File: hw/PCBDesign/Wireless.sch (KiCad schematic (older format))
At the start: 5 parts

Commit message: Clean up schematics some
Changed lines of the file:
@@
 Text HLabel 6300 1100 1    50   Input ~ 0
 V+
+Text HLabel 4550 3600 2    50   Input ~ 0
+BT_VCC_EN
+Text HLabel 4200 1000 0    50   Input ~ 0
+RF24_VCC_EN
 $EndSCHEMATC

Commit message: Schematic polishing
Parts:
- C34: renamed from C?; footprint (none) -> Capacitor_SMD:C_0805_2012Metric; LCSC (none) -> C28323
- C35: renamed from C?; value 100nF -> 100n; footprint (none) -> Capacitor_SMD:C_0402_1005Metric; LCSC (none) -> C1525
- R70, R71: renamed from R?; footprint (none) -> Resistor_SMD:R_0402_1005Metric; LCSC (none) -> C25744
- gave numbers to parts that had none: 1
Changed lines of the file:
@@
 $EndDescr
 $Comp
-L RF:NRF24L01_Breakout U?
+L RF:NRF24L01_Breakout U6
 U 1 1 60458E2E
 P 6300 1700
-F 0 "U?" H 6650 2300 50  0000 L CNN
+F 0 "U6" H 6650 2300 50  0000 L CNN
 F 1 "NRF24L01_Breakout" H 6350 2200 50  0000 L CNN
 F 2 "RF_Module:nRF24L01_Breakout" H 6450 2300 50  0001 L CIN
@@
 nRF24_IRQ
 $Comp
-L power:GND #PWR?
+L power:GND #PWR076
 U 1 1 60625E14
 P 6300 2300
-F 0 "#PWR?" H 6300 2050 50  0001 C CNN
+F 0 "#PWR076" H 6300 2050 50  0001 C CNN
 F 1 "GND" H 6305 2127 50  0000 C CNN
 F 2 "" H 6300 2300 50  0001 C CNN
@@
 nRF24_IRQ
 $Comp
-L Device:C C?
+L Device:C C34
 U 1 1 606288B3
 P 8300 1750
-F 0 "C?" H 8415 1796 50  0000 L CNN
+F 0 "C34" H 8415 1796 50  0000 L CNN
 F 1 "10uF" H 8415 1705 50  0000 L CNN
-F 2 "" H 8338 1600 50  0001 C CNN
+F 2 "Capacitor_SMD:C_0805_2012Metric" H 8338 1600 50  0001 C CNN
 F 3 "~" H 8300 1750 50  0001 C CNN
+F 4 "C28323" H 8300 1750 50  0001 C CNN "LCSC"
 	1    8300 1750
 	1    0    0    -1
 $EndComp
 $Comp
-L Device:C C?
+L Device:C C35
 U 1 1 60628CEA
 P 8700 1750
-F 0 "C?" H 8815 1796 50  0000 L CNN
-F 1 "100nF" H 8815 1705 50  0000 L CNN
-F 2 "" H 8738 1600 50  0001 C CNN
+F 0 "C35" H 8815 1796 50  0000 L CNN
+F 1 "100n" H 8815 1705 50  0000 L CNN
+F 2 "Capacitor_SMD:C_0402_1005Metric" H 8738 1600 50  0001 C CNN
 F 3 "~" H 8700 1750 50  0001 C CNN
+F 4 "C1525" H 8700 1750 50  0001 C CNN "LCSC"
 	1    8700 1750
 	1    0    0    -1
 $EndComp
 $Comp
-L Device:R_US R?
+L Device:R_US R71
 U 1 1 60628F56
 P 7750 1800
-F 0 "R?" H 7818 1846 50  0000 L CNN
+F 0 "R71" H 7818 1846 50  0000 L CNN
 F 1 "10k" H 7818 1755 50  0000 L CNN
-F 2 "" V 7790 1790 50  0001 C CNN
+F 2 "Resistor_SMD:R_0402_1005Metric" V 7790 1790 50  0001 C CNN
 F 3 "~" H 7750 1800 50  0001 C CNN
+F 4 "C25744" H 7750 1800 50  0001 C CNN "LCSC"
 	1    7750 1800
 	0    1    1    0
@@
 	8300 1600 8300 1500
 $Comp
-L power:GND #PWR?
+L power:GND #PWR077
 U 1 1 60629A72
 P 8300 1900
-F 0 "#PWR?" H 8300 1650 50  0001 C CNN
+F 0 "#PWR077" H 8300 1650 50  0001 C CNN
 F 1 "GND" H 8305 1727 50  0000 C CNN
 F 2 "" H 8300 1900 50  0001 C CNN
@@
 $EndComp
 $Comp
-L power:GND #PWR?
+L power:GND #PWR078
 U 1 1 60629F1D
 P 8700 1900
-F 0 "#PWR?" H 8700 1650 50  0001 C CNN
+F 0 "#PWR078" H 8700 1650 50  0001 C CNN
 F 1 "GND" H 8705 1727 50  0000 C CNN
 F 2 "" H 8700 1900 50  0001 C CNN
@@
 	7600 1800 7400 1800
 $Comp
-L Device:R_US R?
+L Device:R_US R70
 U 1 1 6062A636
 P 7750 1500
-F 0 "R?" H 7818 1546 50  0000 L CNN
+F 0 "R70" H 7818 1546 50  0000 L CNN
 F 1 "10k" H 7818 1455 50  0000 L CNN
-F 2 "" V 7790 1490 50  0001 C CNN
+F 2 "Resistor_SMD:R_0402_1005Metric" V 7790 1490 50  0001 C CNN
 F 3 "~" H 7750 1500 50  0001 C CNN
+F 4 "C25744" H 7750 1500 50  0001 C CNN "LCSC"
 	1    7750 1500
 	0    1    1    0

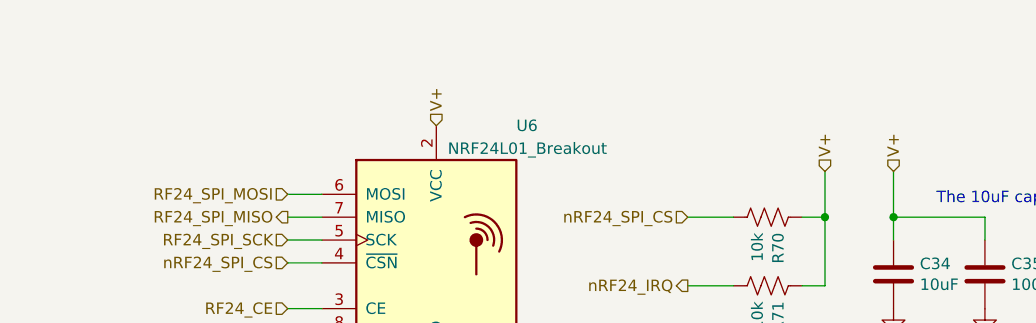
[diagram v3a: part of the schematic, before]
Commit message: Laid out power section
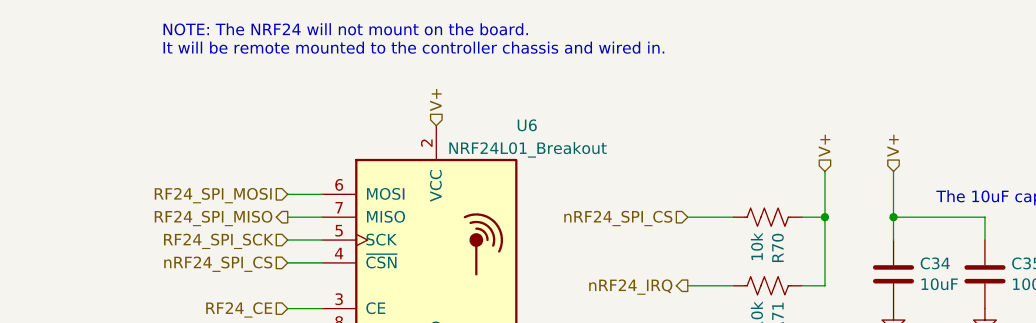
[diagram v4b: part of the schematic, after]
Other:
- note added: "NOTE: The NRF24 will not mount on the board.\nIt will be remote mounted to the controller chassis and wired in."
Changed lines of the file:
@@
 Text HLabel 4200 1000 0    50   Input ~ 0
 RF24_VCC_EN
+Text Notes 5100 800  0    50   ~ 0
+NOTE: The NRF24 will not mount on the board.\nIt will be remote mounted to the controller chassis and wired in.
 $EndSCHEMATC

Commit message: Lay out more PCB
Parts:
- added C58: 100n, Capacitor_SMD:C_0402_1005Metric, symbol Device:C
- added C59: 10uF, Capacitor_SMD:C_0805_2012Metric, symbol Device:C
- added D7: BT_ON, LED_SMD:LED_0603_1608Metric, symbol Device:LED
- added Q2, Q3: si2302, Package_TO_SOT_SMD:SOT-23, symbol Transistor_FET:2N7002
- added Q4, Q5: si2301, Package_TO_SOT_SMD:SOT-23, symbol Transistor_FET:Si2319CDS
- added R100, R56, R58, R59, R98: 10k, Resistor_SMD:R_0402_1005Metric, symbol Device:R_US
- added R101: 560, Resistor_SMD:R_0402_1005Metric, symbol Device:R_US
- added U14: RN4871, RF_Module:Microchip_RN4871, symbol RF_Bluetooth:RN4871
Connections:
- net BT_RX: now also U14.7 (UART_RX)
- net BT_TX: now also U14.8 (UART_TX)
- net BT_VCC_EN: now also Q2.1 (G), R56.2
- net GND: now also C58.2, C59.2, D7.1 (K), Q2.2 (S), Q3.2 (S), R56.1, R58.1, U14.13 (GND), U14.2 (GND)
- net RF24_VCC_EN: now also Q3.1 (G), R58.2
- net V+: now also Q4.2 (S), Q5.2 (S), R59.2, R98.2; no longer C34.1, C35.1, R70.1, R71.1, U6.2 (VCC)
- new net: C34.1, C35.1, Q5.3 (D), R70.1, R71.1, U6.2 (VCC)
- new net: R100.2, U14.10 (RST)
- new net: R101.2, U14.12 (P0_2)
- new net: C58.1, C59.1, Q4.3 (D), R100.1, U14.14 (VBAT)
- new net: Q3.3 (D), Q5.1 (G), R98.1
- new net: Q2.3 (D), Q4.1 (G), R59.1
- new net: D7.2 (A), R101.1
- no-connect marks 0 -> 9
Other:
- note removed: "Need to add symbol for the HM-BT4502 bluetooth radio"

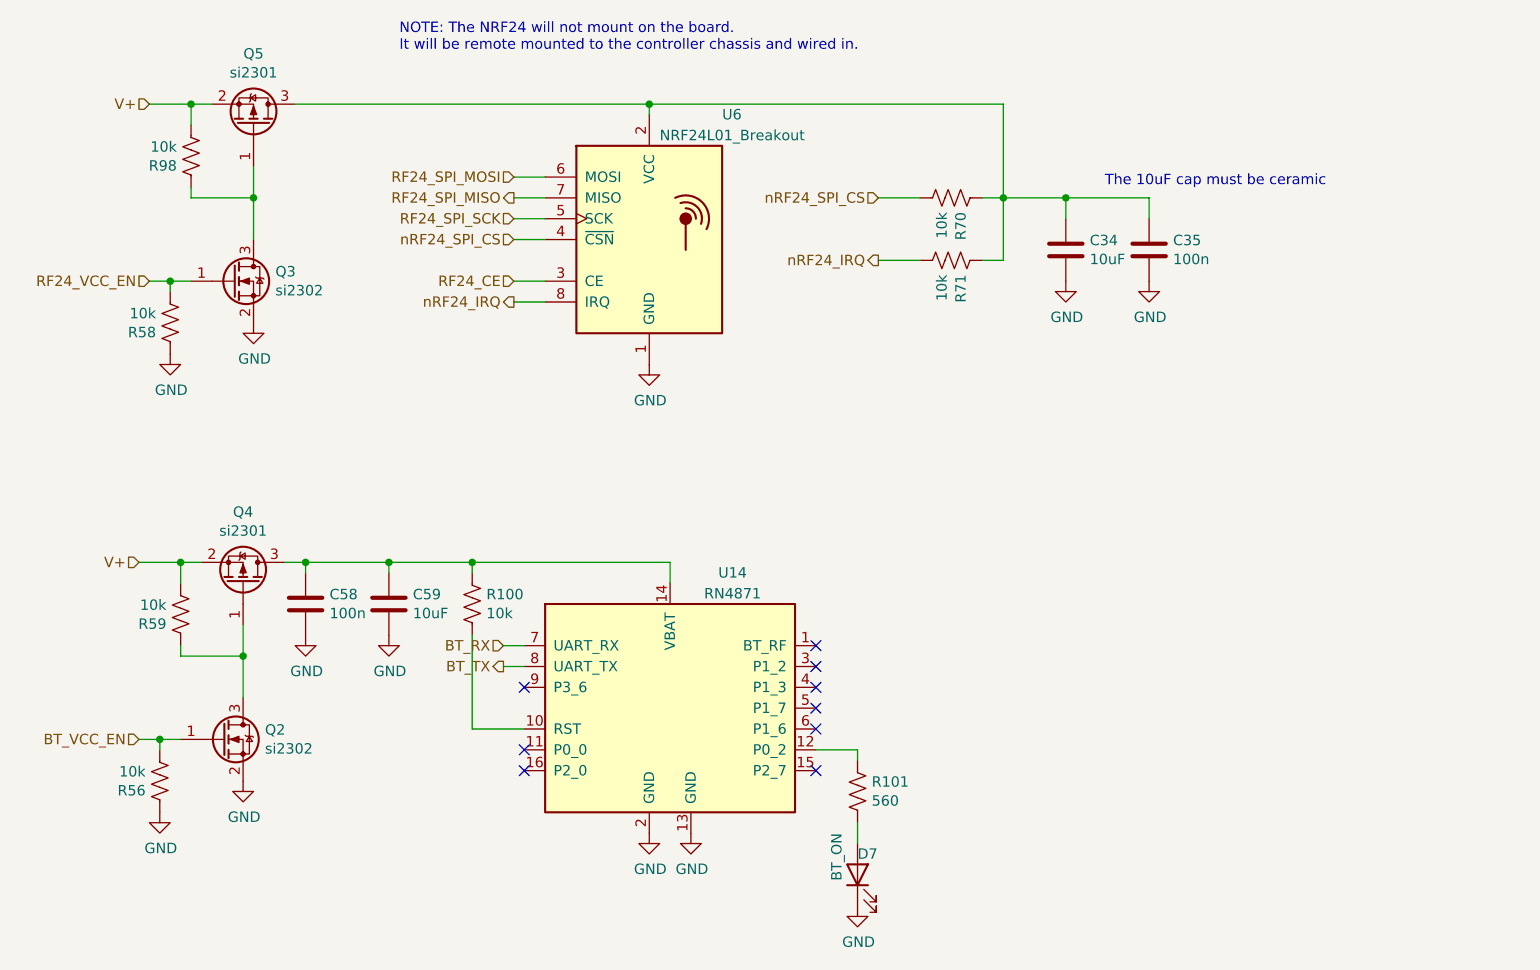
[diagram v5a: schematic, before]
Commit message: Finished preliminary route of PCB after design review checklist
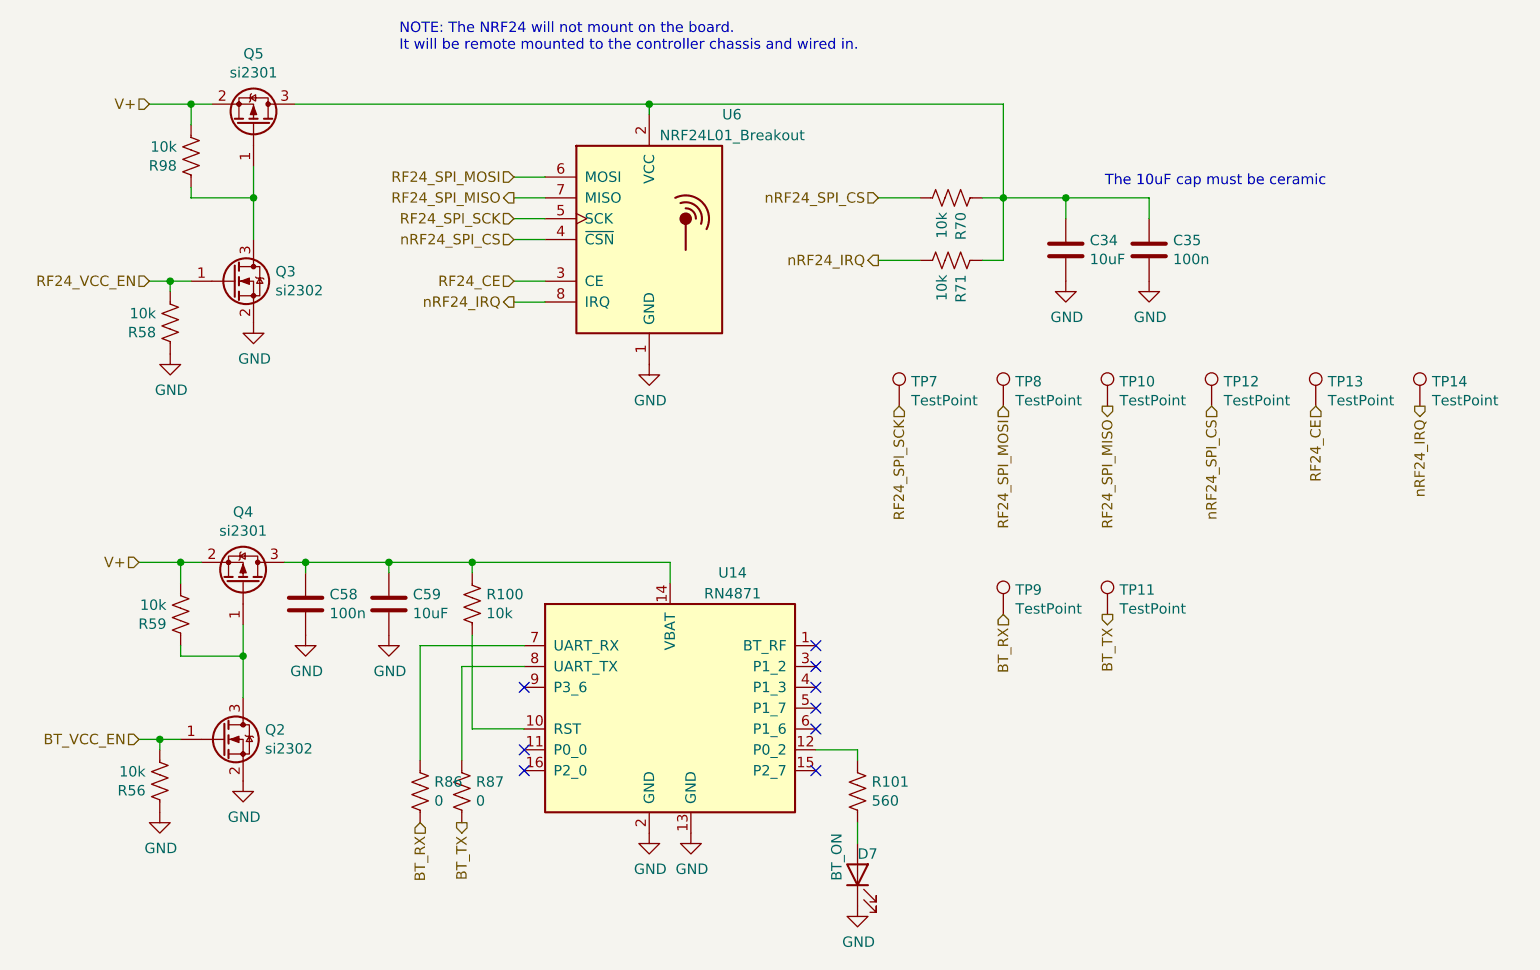
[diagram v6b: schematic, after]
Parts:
- added R86, R87: 0, Resistor_SMD:R_0805_2012Metric, symbol Device:R_US
- added TP10, TP11, TP12, TP13, TP14, TP7, TP8, TP9: TestPoint, TestPoint:TestPoint_Pad_2.5x2.5mm, symbol Connector:TestPoint
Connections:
- net BT_RX: now also R86.2, TP9.1; no longer U14.7 (UART_RX)
- net BT_TX: now also R87.2, TP11.1; no longer U14.8 (UART_TX)
- net RF24_CE: now also TP13.1
- net RF24_SPI_MISO: now also TP10.1
- net RF24_SPI_MOSI: now also TP8.1
- net RF24_SPI_SCK: now also TP7.1
- net nRF24_IRQ: now also TP14.1
- net nRF24_SPI_CS: now also TP12.1
- new net: R86.1, U14.7 (UART_RX)
- new net: R87.1, U14.8 (UART_TX)
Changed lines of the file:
@@
 	1    0    0    -1
 $EndComp
-Text HLabel 5600 3650 0    50   Input ~ 0
+Text HLabel 5200 4500 3    50   Input ~ 0
 BT_RX
-Text HLabel 5600 3750 0    50   Output ~ 0
+Text HLabel 5400 4500 3    50   Output ~ 0
 BT_TX
 Text HLabel 5650 1400 0    50   Input ~ 0
@@
 F 1 "RN4871" H 6700 4500 50  0000 C CNN
 F 2 "RF_Module:Microchip_RN4871" H 6400 3250 50  0001 C CNN
-F 3 "http://ww1.microchip.com/downloads/en/DeviceDoc/50002489A.pdf" H 5900 4500 50  0001 C CNN
+F 3 "http://ww1.microchip.com/downloads/en/DeviceDoc/50002489C.pdf" H 5900 4500 50  0001 C CNN
 	1    6400 3950
 	1    0    0    -1
@@
 $EndComp
 Wire Wire Line
-	5600 3750 5700 3750
-Wire Wire Line
-	5600 3650 5700 3650
-Wire Wire Line
 	4650 3300 4650 3250
 Connection ~ 4650 3250
@@
 Wire Wire Line
 	5450 4050 5700 4050
+$Comp
+L Device:R_US R87
+U 1 1 605A9E3C
+P 5400 4350
+F 0 "R87" H 5468 4396 50  0000 L CNN
+F 1 "0" H 5468 4305 50  0000 L CNN
+F 2 "Resistor_SMD:R_0805_2012Metric" V 5440 4340 50  0001 C CNN
+F 3 "~" H 5400 4350 50  0001 C CNN
+F 4 "C17477" H 5400 4350 50  0001 C CNN "LCSC"
+	1    5400 4350
+	1    0    0    -1
+$EndComp
+$Comp
+L Device:R_US R86
+U 1 1 605AA255
+P 5200 4350
+F 0 "R86" H 5268 4396 50  0000 L CNN
+F 1 "0" H 5268 4305 50  0000 L CNN
+F 2 "Resistor_SMD:R_0805_2012Metric" V 5240 4340 50  0001 C CNN
+F 3 "~" H 5200 4350 50  0001 C CNN
+F 4 "C17477" H 5200 4350 50  0001 C CNN "LCSC"
+	1    5200 4350
+	1    0    0    -1
+$EndComp
+Wire Wire Line
+	5200 4200 5200 3650
+Wire Wire Line
+	5200 3650 5700 3650
+Wire Wire Line
+	5400 3750 5700 3750
+Wire Wire Line
+	5400 3750 5400 4200
+$Comp
+L Connector:TestPoint TP10
+U 1 1 605C7EEC
+P 8500 2500
+F 0 "TP10" H 8558 2618 50  0000 L CNN
+F 1 "TestPoint" H 8558 2527 50  0000 L CNN
+F 2 "TestPoint:TestPoint_Pad_2.5x2.5mm" H 8700 2500 50  0001 C CNN
+F 3 "~" H 8700 2500 50  0001 C CNN
+	1    8500 2500
+	1    0    0    -1
+$EndComp
+$Comp
+L Connector:TestPoint TP12
+U 1 1 605C8193
+P 9000 2500
+F 0 "TP12" H 9058 2618 50  0000 L CNN
+F 1 "TestPoint" H 9058 2527 50  0000 L CNN
+F 2 "TestPoint:TestPoint_Pad_2.5x2.5mm" H 9200 2500 50  0001 C CNN
+F 3 "~" H 9200 2500 50  0001 C CNN
+	1    9000 2500
+	1    0    0    -1
+$EndComp
+$Comp
+L Connector:TestPoint TP13
+U 1 1 605C825C
+P 9500 2500
+F 0 "TP13" H 9558 2618 50  0000 L CNN
+F 1 "TestPoint" H 9558 2527 50  0000 L CNN
+F 2 "TestPoint:TestPoint_Pad_2.5x2.5mm" H 9700 2500 50  0001 C CNN
+F 3 "~" H 9700 2500 50  0001 C CNN
+	1    9500 2500
+	1    0    0    -1
+$EndComp
+$Comp
+L Connector:TestPoint TP14
+U 1 1 605C8384
+P 10000 2500
+F 0 "TP14" H 10058 2618 50  0000 L CNN
+F 1 "TestPoint" H 10058 2527 50  0000 L CNN
+F 2 "TestPoint:TestPoint_Pad_2.5x2.5mm" H 10200 2500 50  0001 C CNN
+F 3 "~" H 10200 2500 50  0001 C CNN
+	1    10000 2500
+	1    0    0    -1
+$EndComp
+$Comp
+L Connector:TestPoint TP8
+U 1 1 605C85FA
+P 8000 2500
+F 0 "TP8" H 8058 2618 50  0000 L CNN
+F 1 "TestPoint" H 8058 2527 50  0000 L CNN
+F 2 "TestPoint:TestPoint_Pad_2.5x2.5mm" H 8200 2500 50  0001 C CNN
+F 3 "~" H 8200 2500 50  0001 C CNN
+	1    8000 2500
+	1    0    0    -1
+$EndComp
+$Comp
+L Connector:TestPoint TP7
+U 1 1 605C875B
+P 7500 2500
+F 0 "TP7" H 7558 2618 50  0000 L CNN
+F 1 "TestPoint" H 7558 2527 50  0000 L CNN
+F 2 "TestPoint:TestPoint_Pad_2.5x2.5mm" H 7700 2500 50  0001 C CNN
+F 3 "~" H 7700 2500 50  0001 C CNN
+	1    7500 2500
+	1    0    0    -1
+$EndComp
+$Comp
+L Connector:TestPoint TP9
+U 1 1 605C8883
+P 8000 3500
+F 0 "TP9" H 8058 3618 50  0000 L CNN
+F 1 "TestPoint" H 8058 3527 50  0000 L CNN
+F 2 "TestPoint:TestPoint_Pad_2.5x2.5mm" H 8200 3500 50  0001 C CNN
+F 3 "~" H 8200 3500 50  0001 C CNN
+	1    8000 3500
+	1    0    0    -1
+$EndComp
+$Comp
+L Connector:TestPoint TP11
+U 1 1 605C8B8B
+P 8500 3500
+F 0 "TP11" H 8558 3618 50  0000 L CNN
+F 1 "TestPoint" H 8558 3527 50  0000 L CNN
+F 2 "TestPoint:TestPoint_Pad_2.5x2.5mm" H 8700 3500 50  0001 C CNN
+F 3 "~" H 8700 3500 50  0001 C CNN
+	1    8500 3500
+	1    0    0    -1
+$EndComp
+Text HLabel 8000 3500 3    50   Input ~ 0
+BT_RX
+Text HLabel 8500 3500 3    50   Output ~ 0
+BT_TX
+Text HLabel 7500 2500 3    50   Input ~ 0
+RF24_SPI_SCK
+Text HLabel 8000 2500 3    50   Input ~ 0
+RF24_SPI_MOSI
+Text HLabel 8500 2500 3    50   Output ~ 0
+RF24_SPI_MISO
+Text HLabel 9000 2500 3    50   Input ~ 0
+nRF24_SPI_CS
+Text HLabel 9500 2500 3    50   Input ~ 0
+RF24_CE
+Text HLabel 10000 2500 3    50   Output ~ 0
+nRF24_IRQ
 $EndSCHEMATC

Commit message: Adjust components for lowest build cost
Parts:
- Q2, Q3: value si2302 -> 2N7002; LCSC C181087 -> C8545
- Q4, Q5: value si2301 -> LBSS84LT1G; LCSC C10487 -> C8492
- U14: DigiKey (none) -> 150-RN4871-I/RM140-ND
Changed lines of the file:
@@
 F 2 "RF_Module:Microchip_RN4871" H 6400 3250 50  0001 C CNN
 F 3 "http://ww1.microchip.com/downloads/en/DeviceDoc/50002489C.pdf" H 5900 4500 50  0001 C CNN
+F 4 "150-RN4871-I/RM140-ND" H 6400 3950 50  0001 C CNN "DigiKey"
 	1    6400 3950
-	1    0    0    -1
-$EndComp
-$Comp
-L Transistor_FET:Si2319CDS Q5
-U 1 1 6059471C
-P 4400 1150
-F 0 "Q5" V 4742 1150 50  0000 C CNN
-F 1 "si2301" V 4651 1150 50  0000 C CNN
-F 2 "Package_TO_SOT_SMD:SOT-23" H 4600 1075 50  0001 L CIN
-F 3 "http://www.vishay.com/docs/66709/si2319cd.pdf" H 4400 1150 50  0001 L CNN
-F 4 "C10487" V 4400 1150 50  0001 C CNN "LCSC"
-	1    4400 1150
-	0    1    -1   0
-$EndComp
-$Comp
-L Transistor_FET:2N7002 Q3
-U 1 1 60595B07
-P 4300 1900
-F 0 "Q3" H 4505 1946 50  0000 L CNN
-F 1 "si2302" H 4505 1855 50  0000 L CNN
-F 2 "Package_TO_SOT_SMD:SOT-23" H 4500 1825 50  0001 L CIN
-F 3 "https://www.onsemi.com/pub/Collateral/NDS7002A-D.PDF" H 4300 1900 50  0001 L CNN
-F 4 "C181087" H 4300 1900 50  0001 C CNN "LCSC"
-	1    4300 1900
 	1    0    0    -1
 $EndComp
@@
 P 4350 3350
 F 0 "Q4" V 4692 3350 50  0000 C CNN
-F 1 "si2301" V 4601 3350 50  0000 C CNN
+F 1 "LBSS84LT1G" V 4601 3350 50  0000 C CNN
 F 2 "Package_TO_SOT_SMD:SOT-23" H 4550 3275 50  0001 L CIN
-F 3 "http://www.vishay.com/docs/66709/si2319cd.pdf" H 4350 3350 50  0001 L CNN
-F 4 "C10487" V 4350 3350 50  0001 C CNN "LCSC"
+F 3 "https://datasheet.lcsc.com/szlcsc/Leshan-Radio-LBSS84LT1G_C8492.pdf" H 4350 3350 50  0001 L CNN
+F 4 "C8492" V 4350 3350 50  0001 C CNN "LCSC"
 	1    4350 3350
 	0    1    -1   0
-$EndComp
-$Comp
-L Transistor_FET:2N7002 Q2
-U 1 1 6059FCBC
-P 4250 4100
-F 0 "Q2" H 4455 4146 50  0000 L CNN
-F 1 "si2302" H 4455 4055 50  0000 L CNN
-F 2 "Package_TO_SOT_SMD:SOT-23" H 4450 4025 50  0001 L CIN
-F 3 "https://www.onsemi.com/pub/Collateral/NDS7002A-D.PDF" H 4250 4100 50  0001 L CNN
-F 4 "C181087" H 4250 4100 50  0001 C CNN "LCSC"
-	1    4250 4100
-	1    0    0    -1
 $EndComp
 Text HLabel 3850 3250 0    50   Input ~ 0
@@
 Text HLabel 10000 2500 3    50   Output ~ 0
 nRF24_IRQ
+$Comp
+L Transistor_FET:2N7002 Q2
+U 1 1 606243F5
+P 4250 4100
+F 0 "Q2" H 4454 4146 50  0000 L CNN
+F 1 "2N7002" H 4454 4055 50  0000 L CNN
+F 2 "Package_TO_SOT_SMD:SOT-23" H 4450 4025 50  0001 L CIN
+F 3 "https://www.onsemi.com/pub/Collateral/NDS7002A-D.PDF" H 4250 4100 50  0001 L CNN
+F 4 "C8545" H 4250 4100 50  0001 C CNN "LCSC"
+	1    4250 4100
+	1    0    0    -1
+$EndComp
+$Comp
+L Transistor_FET:2N7002 Q3
+U 1 1 60626AC3
+P 4300 1900
+F 0 "Q3" H 4504 1946 50  0000 L CNN
+F 1 "2N7002" H 4504 1855 50  0000 L CNN
+F 2 "Package_TO_SOT_SMD:SOT-23" H 4500 1825 50  0001 L CIN
+F 3 "https://www.onsemi.com/pub/Collateral/NDS7002A-D.PDF" H 4300 1900 50  0001 L CNN
+F 4 "C8545" H 4300 1900 50  0001 C CNN "LCSC"
+	1    4300 1900
+	1    0    0    -1
+$EndComp
+$Comp
+L Transistor_FET:Si2319CDS Q5
+U 1 1 60629D20
+P 4400 1150
+F 0 "Q5" V 4742 1150 50  0000 C CNN
+F 1 "LBSS84LT1G" V 4651 1150 50  0000 C CNN
+F 2 "Package_TO_SOT_SMD:SOT-23" H 4600 1075 50  0001 L CIN
+F 3 "https://datasheet.lcsc.com/szlcsc/Leshan-Radio-LBSS84LT1G_C8492.pdf" H 4400 1150 50  0001 L CNN
+F 4 "C8492" V 4400 1150 50  0001 C CNN "LCSC"
+	1    4400 1150
+	0    1    -1   0
+$EndComp
 $EndSCHEMATC
